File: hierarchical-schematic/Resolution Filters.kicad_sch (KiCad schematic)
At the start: 55 parts, among them J310 Conn_Coaxial, J311 Terminal Block, J312 Conn_Coaxial, K301 G5V-1, K302 G5V-1, SW301 SW_SPST, T302 Transformer_1P_1S, T303 Transformer_1P_1S, Y301 10.7MHz, Y302 10.7MHz, Y303 10.7MHz, Y304 10.7MHz

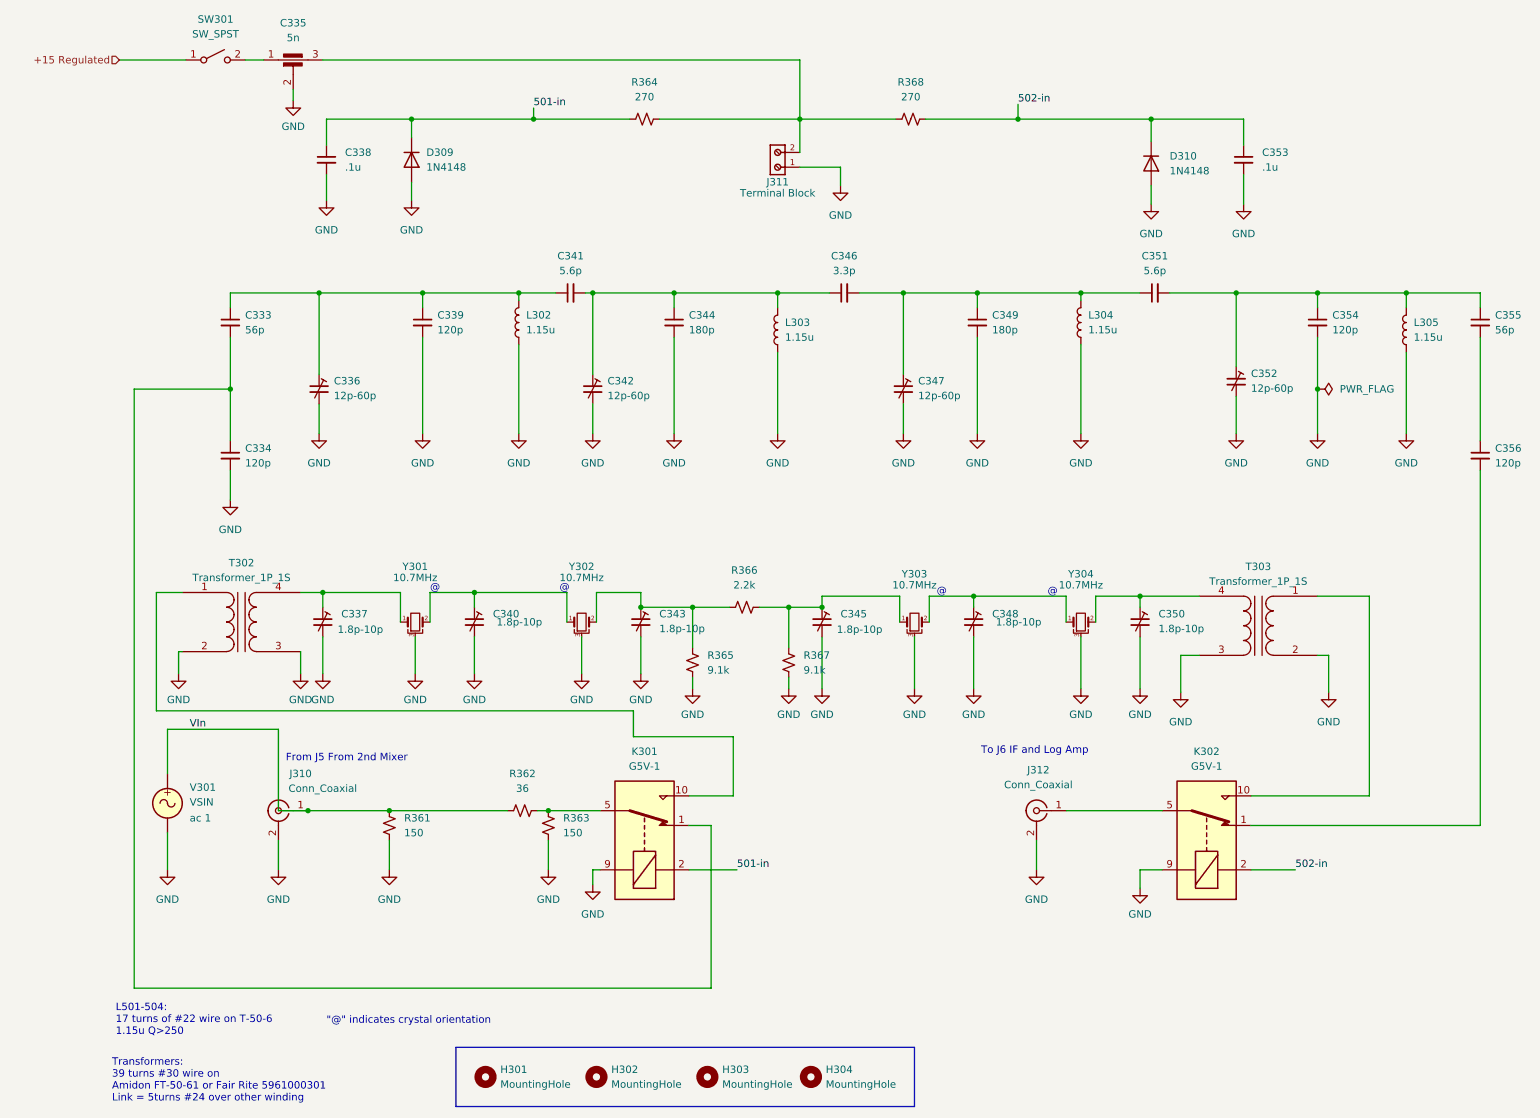
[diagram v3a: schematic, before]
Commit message: Hierarchical schematic updates
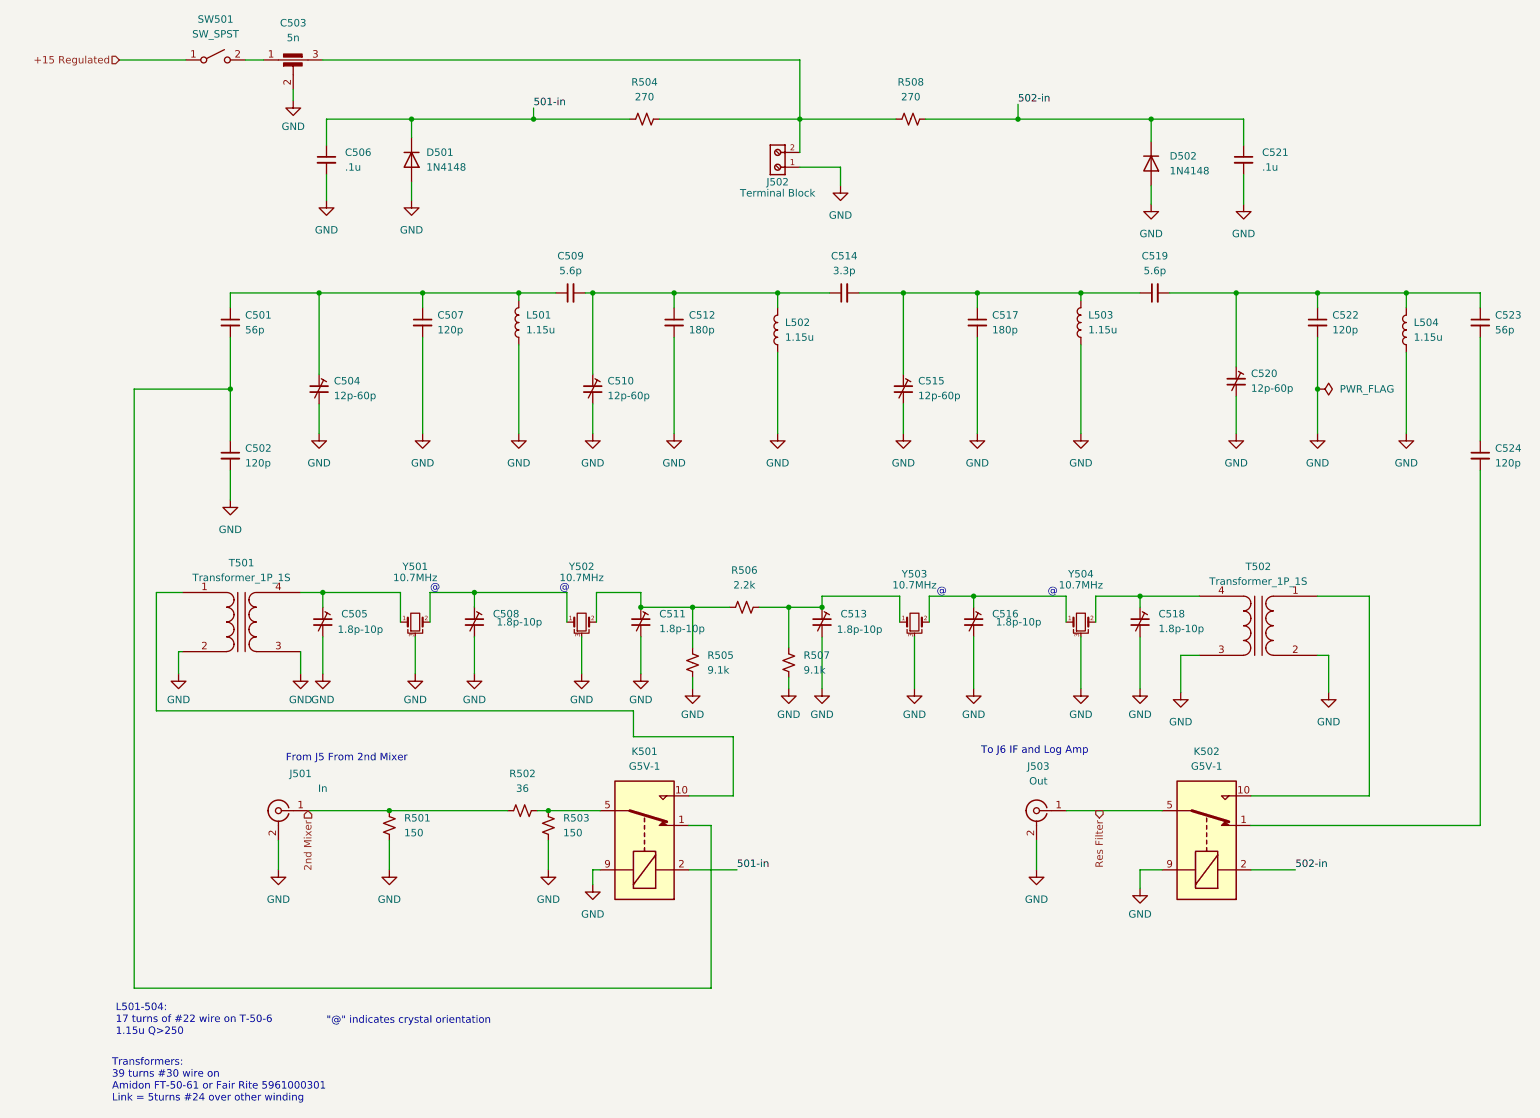
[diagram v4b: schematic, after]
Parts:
- removed H301, H302, H303, H304: MountingHole, MountingHole:MountingHole_3.2mm_M3, symbol Mechanical:MountingHole
- removed V301: VSIN, symbol Simulation_SPICE:VSIN
- J501: renamed from J310; value Conn_Coaxial -> In
- J503: renamed from J312; value Conn_Coaxial -> Out
- renumbered C333 to C501, C334 to C502, C335 to C503, C336 to C504, C337 to C505, C338 to C506, C339 to C507, C340 to C508, C341 to C509, C342 to C510, C343 to C511, C344 to C512, C345 to C513, C346 to C514, C347 to C515, C348 to C516, C349 to C517, C350 to C518, C351 to C519, C352 to C520, C353 to C521, C354 to C522, C355 to C523, C356 to C524, D309 to D501, D310 to D502, J311 to J502, K301 to K501, K302 to K502, L302 to L501, L303 to L502, L304 to L503, L305 to L504, R361 to R501, R362 to R502, R363 to R503, R364 to R504, R365 to R505, R366 to R506, R367 to R507, R368 to R508, SW301 to SW501, T302 to T501, T303 to T502, Y301 to Y501, Y302 to Y502, Y303 to Y503, Y304 to Y504
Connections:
- net Res Filter: now reaches J503.1 (In), K502.5, K502.6
- net VIn renamed 2nd Mixer

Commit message: hierarchical schematic updated to pass erc
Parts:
- J502: footprint resolution-filters:691137710002 -> 691137710002; symbol 691137710002:691137710002 -> spectrum analyzer:691137710002
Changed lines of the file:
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@@
   (junction (at 102.87 32.385) (diameter 0) (color 0 0 0 0)
   )
-  (junction (at 258.445 78.74) (diameter 0) (color 0 0 0 0)
-  )
   (junction (at 167.64 116.205) (diameter 0) (color 0 0 0 0)
   )
@@
     (stroke (width 0) (type default) (color 0 0 0 0))
   )
-  (wire (pts (xy 258.445 78.74) (xy 258.445 86.36))
+  (wire (pts (xy 258.445 69.85) (xy 258.445 86.36))
     (stroke (width 0) (type default) (color 0 0 0 0))
   )
@@
   )
   (wire (pts (xy 147.955 64.77) (xy 147.955 62.23))
-    (stroke (width 0) (type default) (color 0 0 0 0))
-  )
-  (wire (pts (xy 258.445 69.85) (xy 258.445 78.74))
     (stroke (width 0) (type default) (color 0 0 0 0))
   )
@@
     (pin "1")
   )
-  (symbol (lib_id "691137710002:691137710002") (at 164.465 38.1 90) (unit 1)
+  (symbol (lib_id "spectrum analyzer:691137710002") (at 164.465 38.1 90) (unit 1)
     (in_bom yes) (on_board yes)
     (property "Reference" "J502" (id 0) (at 165.735 43.18 90))
     (property "Value" "Terminal Block" (id 1) (at 165.735 45.085 90))
-    (property "Footprint" "resolution-filters:691137710002" (id 2) (at 164.465 38.1 0)
+    (property "Footprint" "691137710002" (id 2) (at 164.465 38.1 0)
       (effects (font (size 1.27 1.27)) (justify left bottom) hide)
     )
@@
     (pin "2")
   )
-  (symbol (lib_id "power:PWR_FLAG") (at 258.445 78.74 270) (unit 1)
-    (in_bom yes) (on_board yes) (fields_autoplaced)
-    (property "Reference" "#FLG0501" (id 0) (at 260.35 78.74 0)
-      (effects (font (size 1.27 1.27)) hide)
-    )
-    (property "Value" "PWR_FLAG" (id 1) (at 262.255 78.7399 90)
-      (effects (font (size 1.27 1.27)) (justify left))
-    )
-    (property "Footprint" "" (id 2) (at 258.445 78.74 0)
-      (effects (font (size 1.27 1.27)) hide)
-    )
-    (property "Datasheet" "~" (id 3) (at 258.445 78.74 0)
-      (effects (font (size 1.27 1.27)) hide)
-    )
-    (pin "1")
-  )
   (symbol (lib_id "Device:L") (at 121.285 67.31 0) (mirror y) (unit 1)

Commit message: v7 conversion
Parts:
- J501, J503: Spice_Model Conn_Coaxial -> (none); Spice_Netlist_Enabled N -> (none); Spice_Primitive J -> (none)
- J502: Spice_Model Terminal Block -> (none); Spice_Netlist_Enabled N -> (none); Spice_Primitive J -> (none)
